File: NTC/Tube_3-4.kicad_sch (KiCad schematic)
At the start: 61 parts, among them Q25 MPSA42, Q26 MPSA42, Q27 MPSA42, Q28 MPSA42, Q29 MPSA42, Q30 MPSA42, Q31 MPSA42, Q32 MPSA42, Q33 MPSA42, Q34 MPSA42, Q35 MPSA42, Q36 MPSA42, Q37 MPSA42, Q38 MPSA42, Q39 MPSA42, Q40 MPSA42, Q41 MPSA42, Q42 MPSA42, Q43 MPSA42, Q44 MPSA42, Q45 MPSA42, Q46 MPSA42, X12 Conn_01x06_Socket, X13 Conn_01x06_Socket, X14 Conn_01x06_Socket, X15 Conn_01x06_Socket

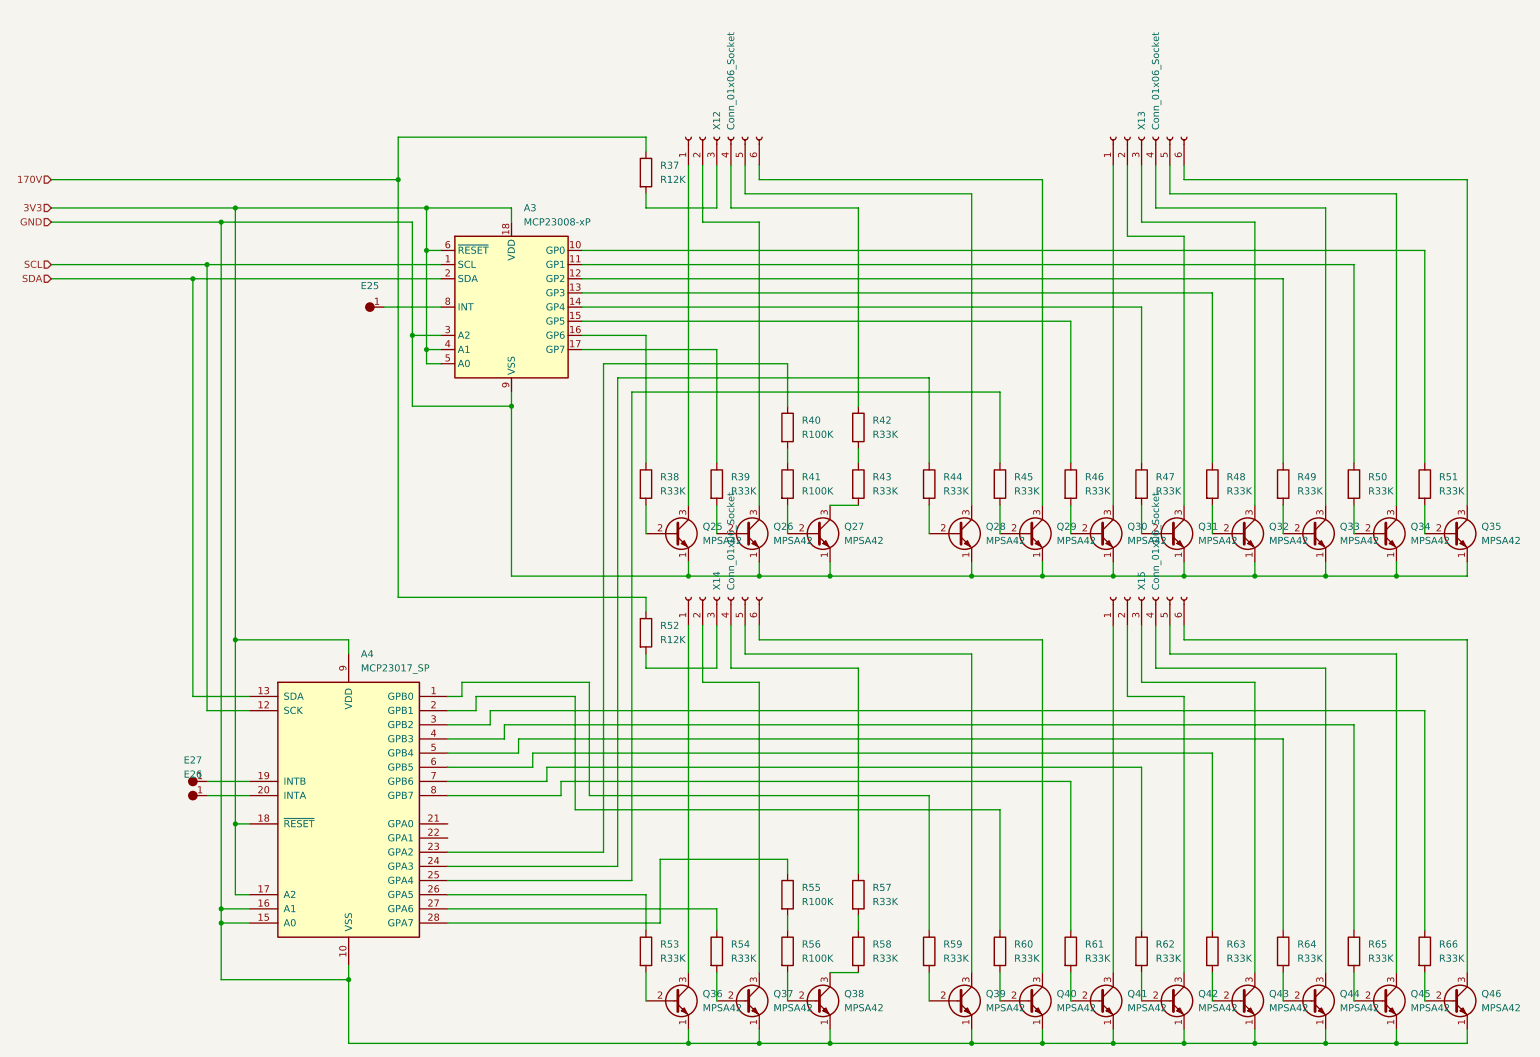
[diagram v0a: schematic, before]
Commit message: Changed to 14pin socket
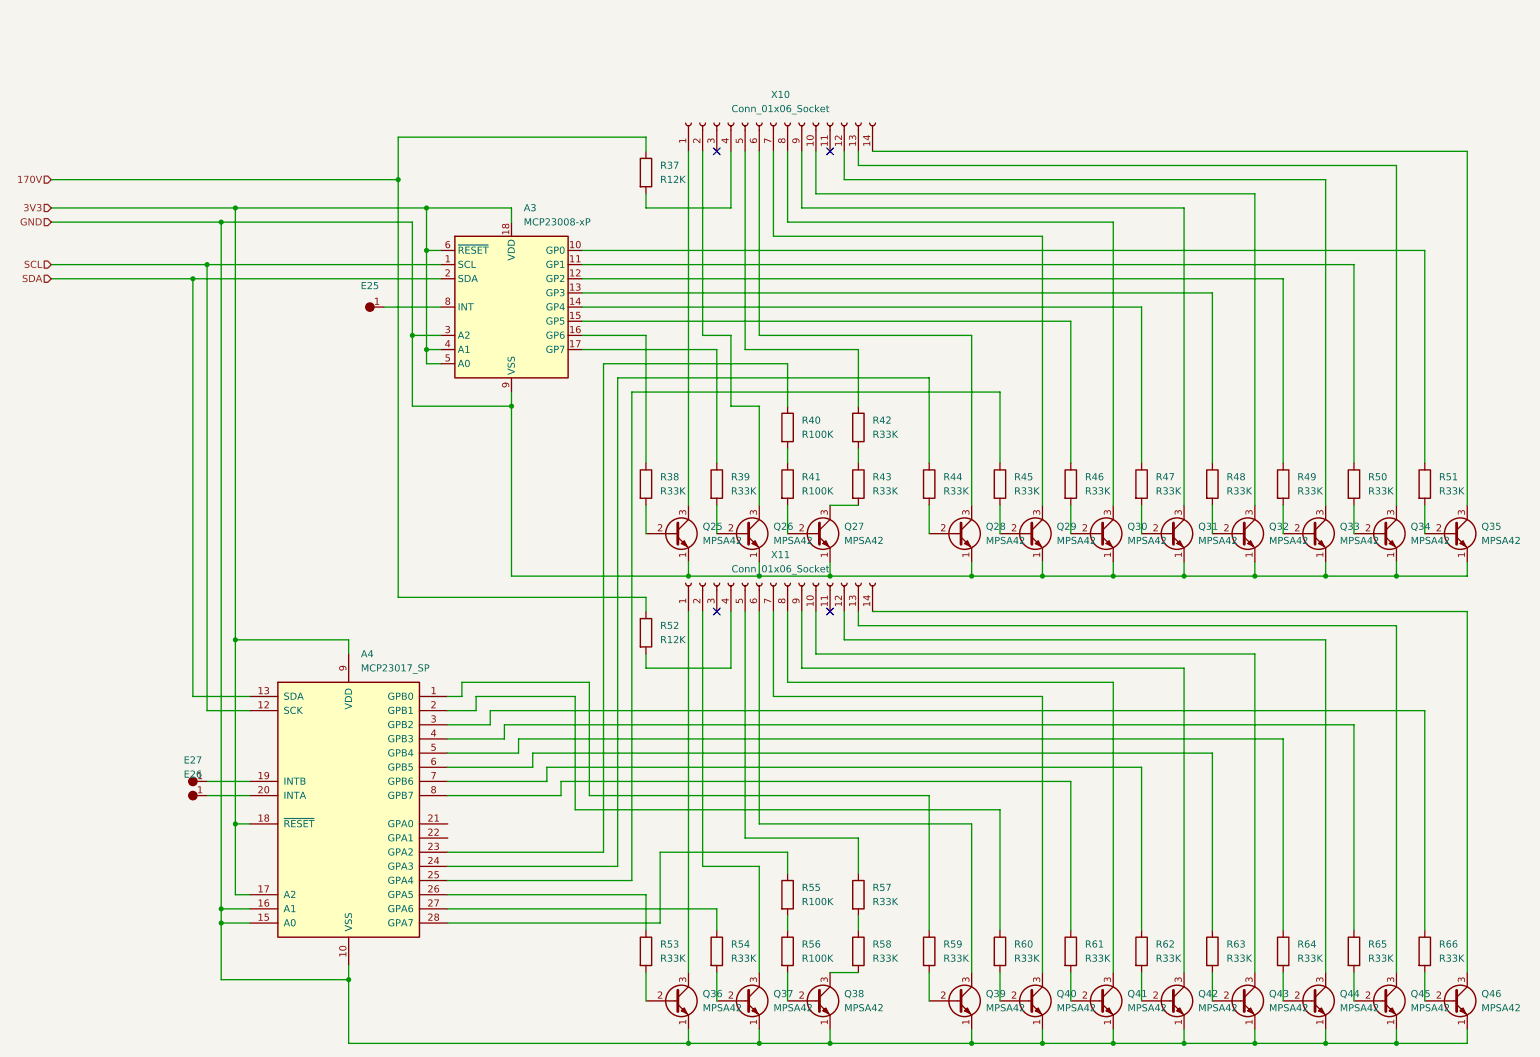
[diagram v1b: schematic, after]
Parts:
- removed X13, X15: Conn_01x06_Socket, Nixie:Pinbar_1-6-f-b, symbol Connector:Conn_01x06_Socket
- A3: footprint Package_DIP:DIP-18_W7.62mm -> Nixie:DIP-18_IC+Socket
- A4: footprint Package_DIP:DIP-28_W7.62mm -> Nixie:DIP-28_IC+Socket
- Q25, Q26, Q27, Q28, Q29, Q30, Q31, Q32, Q33, Q34, Q35, Q36, Q37, Q38, Q39, Q40, Q41, Q42, Q43, Q44, Q45, Q46: footprint Package_TO_SOT_THT:TO-92_Inline -> Nixie:MPSA-42
- X10: renamed from X12; footprint Nixie:Pinbar_1-6-f-a -> Nixie:Pinbar_4-14-f; symbol Connector:Conn_01x06_Socket -> Connector:Conn_01x14_Socket
- X11: renamed from X14; footprint Nixie:Pinbar_1-6-f-a -> Nixie:Pinbar_4-14-f; symbol Connector:Conn_01x06_Socket -> Connector:Conn_01x14_Socket
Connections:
- net at X10.3 (Pin_3): no longer R37.2
- net at X10.4 (Pin_4): now also R37.2; no longer R42.1
- net at X10.5 (Pin_5): now also R42.1; no longer Q28.3 (C)
- net at X10.6 (Pin_6): now also Q28.3 (C); no longer Q29.3 (C)
- net at Q33.3 (C): now also X10.12 (Pin_12)
- net at Q30.3 (C): now also X10.8 (Pin_8)
- net at Q31.3 (C): now also X10.9 (Pin_9)
- net at Q32.3 (C): now also X10.10 (Pin_10)
- net at Q34.3 (C): now also X10.13 (Pin_13)
- net at Q35.3 (C): now also X10.14 (Pin_14)
- net at R57.1: now also X11.5 (Pin_5); no longer X11.4 (Pin_4)
- net at X11.3 (Pin_3): no longer R52.2
- net at Q39.3 (C): now also X11.6 (Pin_6); no longer X11.5 (Pin_5)
- net at Q40.3 (C): now also X11.7 (Pin_7); no longer X11.6 (Pin_6)
- net at Q43.3 (C): now also X11.10 (Pin_10)
- net at Q41.3 (C): now also X11.8 (Pin_8)
- net at Q42.3 (C): now also X11.9 (Pin_9)
- net at Q44.3 (C): now also X11.12 (Pin_12)
- net at Q45.3 (C): now also X11.13 (Pin_13)
- net at Q46.3 (C): now also X11.14 (Pin_14)
- new net: Q29.3 (C), X10.7 (Pin_7)
- new net: R52.2, X11.4 (Pin_4)
- no-connect marks 0 -> 4

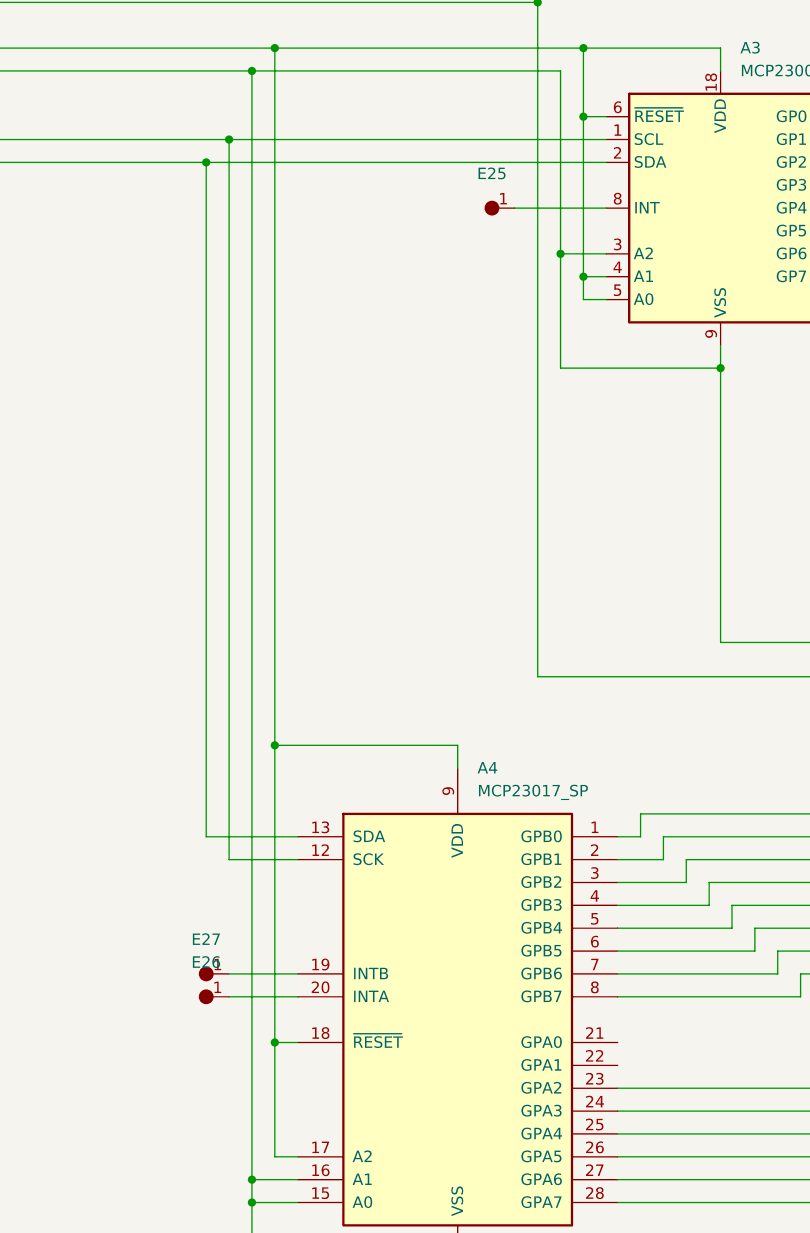
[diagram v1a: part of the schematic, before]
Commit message: Added GPS
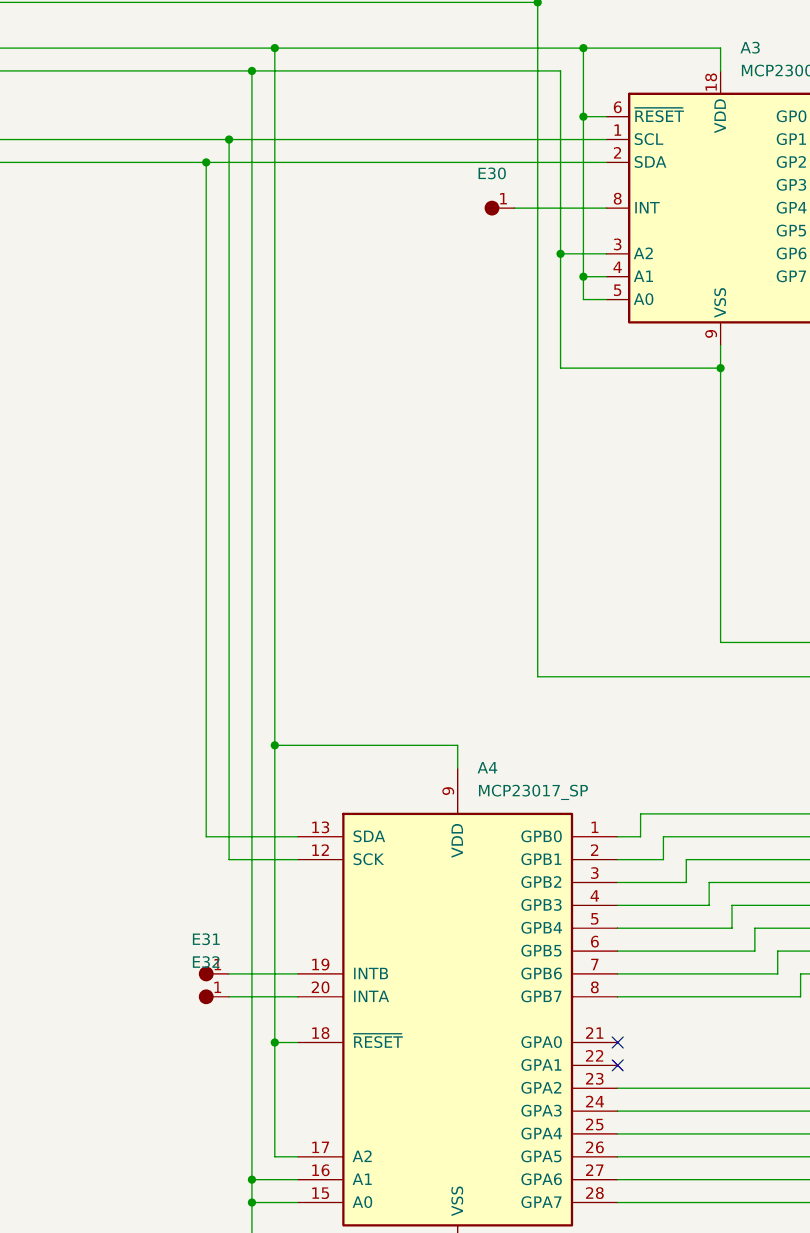
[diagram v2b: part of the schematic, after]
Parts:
- renumbered E25 to E30, E27 to E31, E26 to E32
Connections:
- no-connect marks 4 -> 6
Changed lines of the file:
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@@
 	)
 	(no_connect
+		(at 90.17 139.7)
+	)
+	(no_connect
+		(at 90.17 137.16)
+	)
+	(no_connect
 		(at 158.75 99.06)
 	)
@@
 		(dnp no)
 		(fields_autoplaced yes)
-		(property "Reference" "E27"
+		(property "Reference" "E31"
 			(at 44.45 125.73 0)
 			(effects
@@
 			(project ""
 				(path "/ecf22f8e-0676-4495-9357-338c1fd23f92/4a683942-1315-4074-8a4e-e71a8a4c1705"
-					(reference "E27")
+					(reference "E31")
 					(unit 1)
 				)
@@
 		(dnp no)
 		(fields_autoplaced yes)
-		(property "Reference" "E26"
+		(property "Reference" "E32"
 			(at 44.45 128.27 0)
 			(effects
@@
 			(project ""
 				(path "/ecf22f8e-0676-4495-9357-338c1fd23f92/4a683942-1315-4074-8a4e-e71a8a4c1705"
-					(reference "E26")
+					(reference "E32")
 					(unit 1)
 				)
@@
 		(dnp no)
 		(fields_autoplaced yes)
-		(property "Reference" "E25"
+		(property "Reference" "E30"
 			(at 76.2 40.64 0)
 			(effects
@@
 			(project ""
 				(path "/ecf22f8e-0676-4495-9357-338c1fd23f92/4a683942-1315-4074-8a4e-e71a8a4c1705"
-					(reference "E25")
+					(reference "E30")
 					(unit 1)
 				)
